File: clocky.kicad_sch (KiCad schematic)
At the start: 79 parts, among them J1 Bot 50 pin, J2 Bot 40 pin, J3 Top 50 pin, J4 Top 40 pin, J5 Power, J6 CAP, J8 Skedd, U1 HEF4094B, U10 TMP117xxDRV, U11 ENS220, U2 HEF4094B, U3 HEF4094B, U4 HEF4094B, U5 HEF4094B, U6 HEF4094B, U7 BQ25570, U8 ENS212, U9 STM32U031C8Ux, U98 TMP117xxDRV, U99 TMP117xxDRV, Y1 32768Hz

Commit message: Update PCB layout.  Song and dance with Kicad breaking footprints...
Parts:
- U7: footprint Package_DFN_QFN:QFN-20-1EP_3.5x3.5mm_P0.5mm_EP2x2mm -> Parts:QFN-20-1EP_3.5x3.5mm_P0.5mm_EP2x2mm
- U9: footprint Package_DFN_QFN:QFN-48-1EP_7x7mm_P0.5mm_EP5.6x5.6mm -> Parts:QFN-48-1EP_7x7mm_P0.5mm_EP5.6x5.6mm
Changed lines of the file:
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@@
 			)
 		)
-		(property "Footprint" "Package_DFN_QFN:QFN-48-1EP_7x7mm_P0.5mm_EP5.6x5.6mm"
+		(property "Footprint" "Parts:QFN-48-1EP_7x7mm_P0.5mm_EP5.6x5.6mm"
 			(at 49.53 157.48 0)
 			(effects
@@
 			)
 		)
-		(property "Footprint" "Package_DFN_QFN:QFN-20-1EP_3.5x3.5mm_P0.5mm_EP2x2mm"
+		(property "Footprint" "Parts:QFN-20-1EP_3.5x3.5mm_P0.5mm_EP2x2mm"
 			(at 67.31 53.34 0)
 			(effects

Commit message: Manufacturing updates.
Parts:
- C16: JLCPCB (none) -> C15195; LCSC C15195 -> (none)
- C8: JLCPCB C15850 -> C19702
- R25: value 330k -> 560k; JLCPCB C22807 -> C23203
- U11, U8: now left out of the parts list
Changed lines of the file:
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@@
 			)
 		)
-		(property "LCSC" "C15195"
+		(property "JLCPCB" "C15195"
 			(at 87.63 156.21 0)
 			(effects
@@
 			)
 		)
-		(property "JLCPCB" "C15850"
+		(property "JLCPCB" "C19702"
 			(at 58.42 24.13 0)
 			(effects
@@
 			)
 		)
-		(property "Sim.Pins" "1=K 2=A"
-			(at 96.52 124.46 0)
-			(effects
-				(font
-					(size 1.27 1.27)
-				)
-				(hide yes)
-			)
-		)
 		(property "JLCPCB" "C2290"
 			(at 96.52 124.46 0)
@@
 		(unit 1)
 		(exclude_from_sim no)
-		(in_bom yes)
+		(in_bom no)
 		(on_board yes)
 		(dnp no)
@@
 			)
 		)
-		(property "Value" "330k"
+		(property "Value" "560k"
 			(at 119.38 50.8 90)
 			(effects
@@
 			)
 		)
-		(property "JLCPCB" "C22807"
+		(property "JLCPCB" "C23203"
 			(at 119.38 50.8 0)
 			(effects
@@
 		(unit 1)
 		(exclude_from_sim no)
-		(in_bom yes)
+		(in_bom no)
 		(on_board yes)
 		(dnp no)

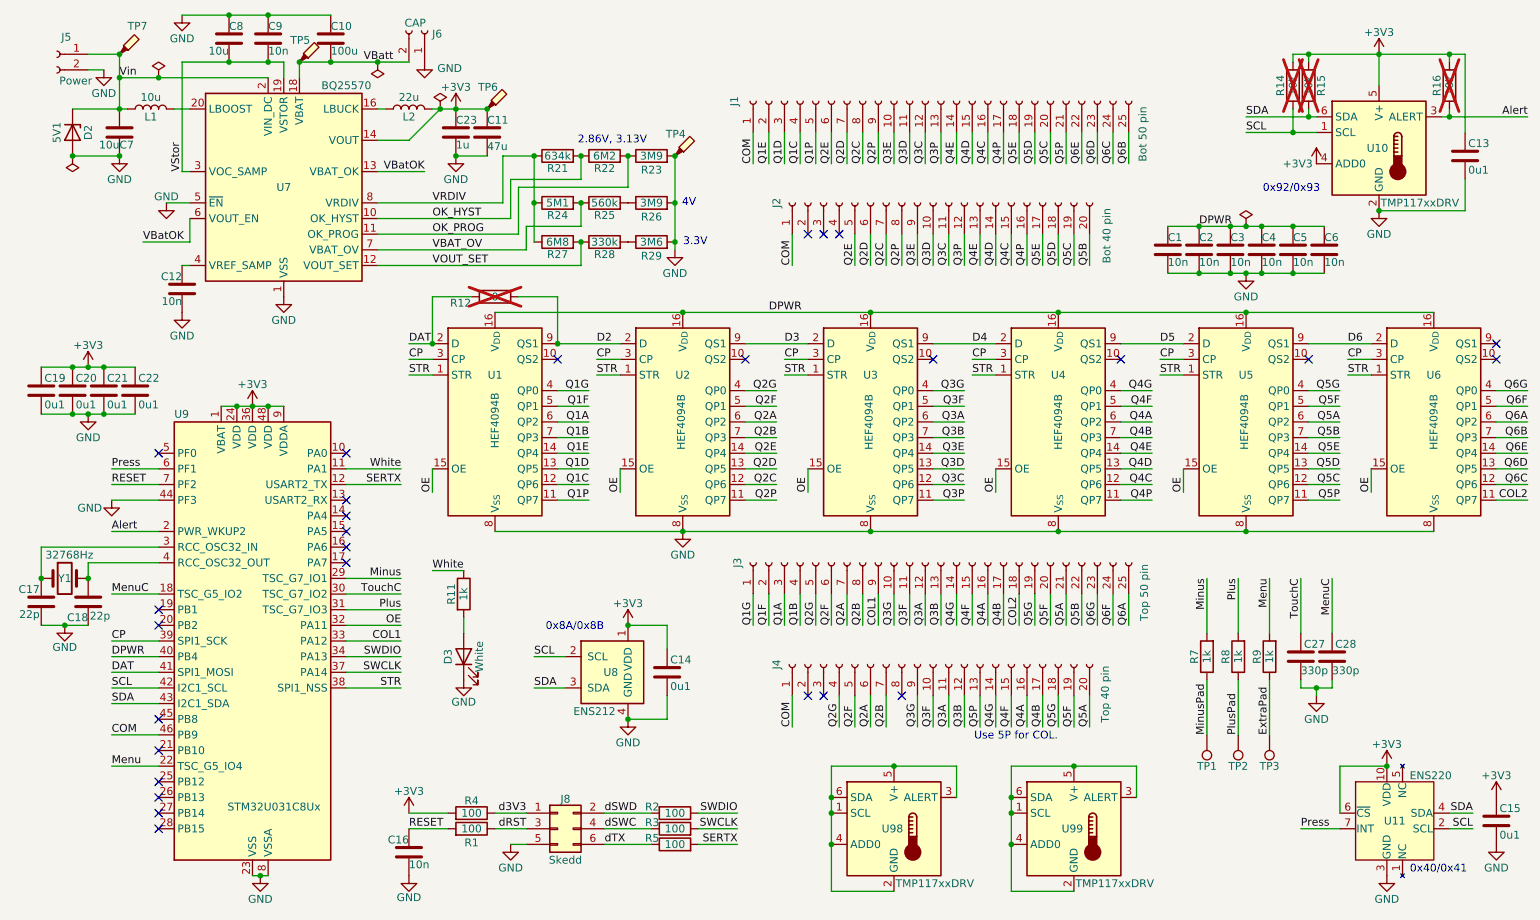
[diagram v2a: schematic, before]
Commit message: Update board with 1.8V power domain.
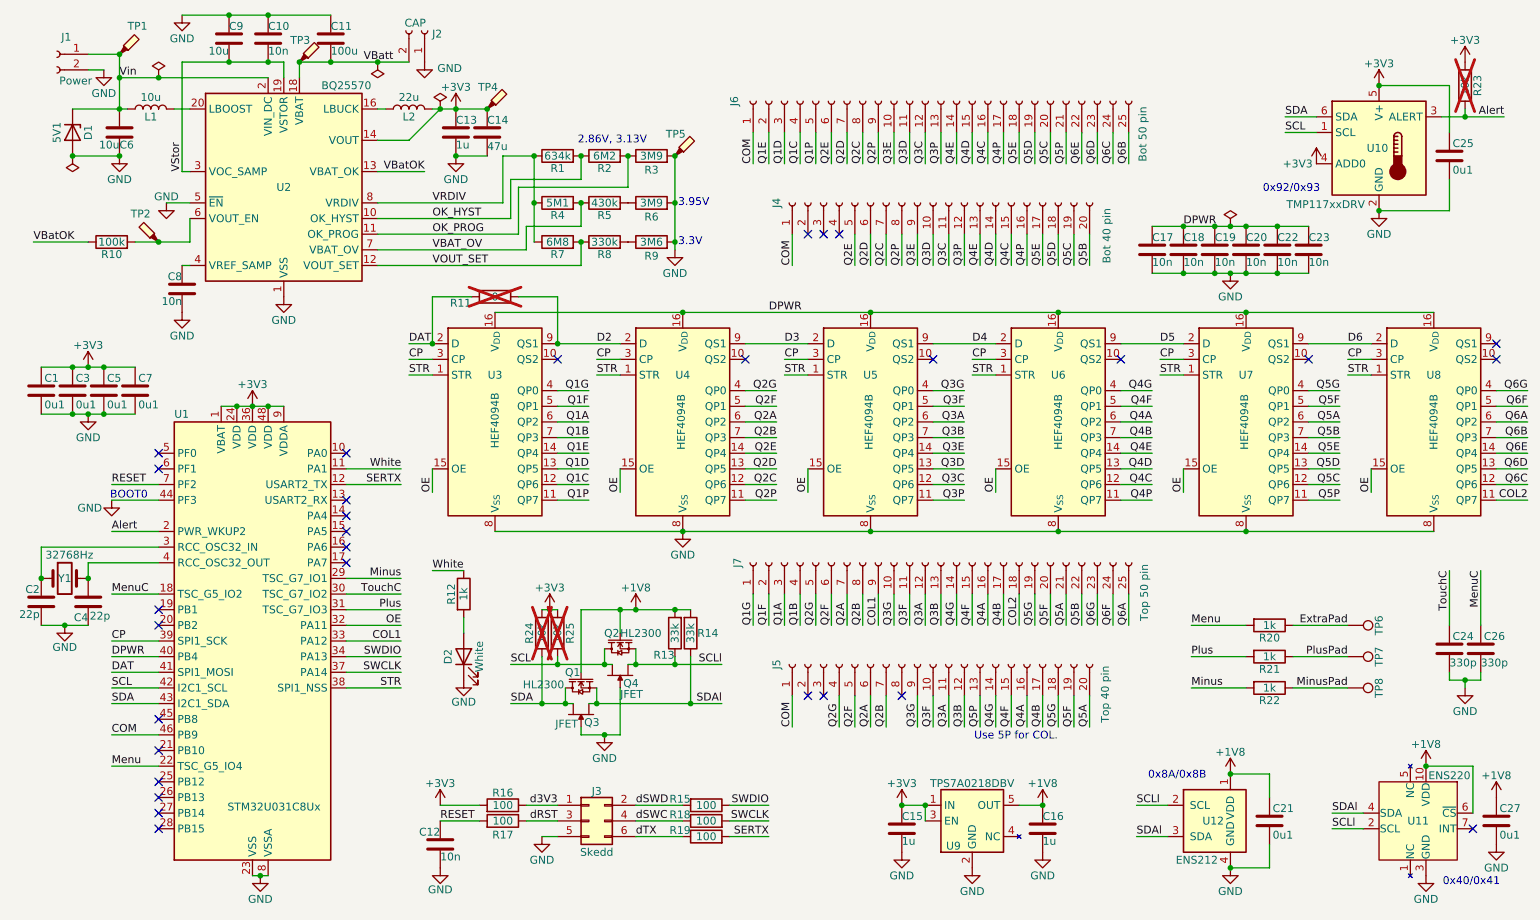
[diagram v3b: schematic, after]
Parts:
- removed U98, U99: TMP117xxDRV, Parts:WSON-6-1EP_2x2mm_P0.65mm_NoEP, symbol Sensor_Temperature:TMP117xxDRV
- added C15, C16: 1u, Capacitor_SMD:C_0402_1005Metric, symbol Device:C
- added Q1, Q2: HL2300, Package_TO_SOT_SMD:SOT-23, symbol Parts:HL2300
- added Q3, Q4: JFET, Package_TO_SOT_SMD:SOT-23-3, symbol Parts:Q_NJFET_DSG
- added R10: 100k, Resistor_SMD:R_0402_1005Metric, symbol Device:R
- added R13, R14: 33k, Resistor_SMD:R_0603_1608Metric, symbol Device:R
- added TP2: TestPoint_Probe, Parts:TestPoint, symbol Connector:TestPoint_Probe
- added U9: TPS7A0218DBV, Package_TO_SOT_SMD:SOT-23-5, symbol Parts:TPS7A0218DBV
- R5: renamed from R25; value 560k -> 430k
- U10: now left out of the parts list
- U2: renamed from U7; now left out of the parts list
- renumbered C19 to C1, C9 to C10, C10 to C11, C16 to C12, C23 to C13, C11 to C14, C1 to C17, C2 to C18, C3 to C19, C17 to C2, C4 to C20, C14 to C21, C5 to C22, C6 to C23, C27 to C24, C13 to C25, C28 to C26, C15 to C27, C20 to C3, C18 to C4, C21 to C5, C7 to C6, C22 to C7, C12 to C8, C8 to C9, D2 to D1, D3 to D2, J5 to J1, J6 to J2, J8 to J3, J2 to J4, J4 to J5, J1 to J6, J3 to J7, R21 to R1, R12 to R11, R11 to R12, R2 to R15, R4 to R16, R1 to R17, R3 to R18, R5 to R19, R22 to R2, R9 to R20, R8 to R21, R7 to R22, R16 to R23, R15 to R24, R14 to R25, R23 to R3, R24 to R4, R26 to R6, R27 to R7, R28 to R8, R29 to R9, TP7 to TP1, TP5 to TP3, TP6 to TP4, TP4 to TP5, TP3 to TP6, TP2 to TP7, TP1 to TP8, U9 to U1, U8 to U12, U1 to U3, U2 to U4, U3 to U5, U4 to U6, U5 to U7, U6 to U8
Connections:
- net +3V3: now also C15.1, U9.1 (IN), U9.3 (EN); no longer C21.1, C27.1, U11.10 (VDD), U11.6 (~{CS}), U12.1 (VDD)
- net GND: now also C15.2, C16.2, Q3.3 (G), Q4.3 (G), U9.2 (GND)
- net SCL: now also Q2.3 (D), Q4.2 (S); no longer U11.2 (SCL), U12.2 (SCL)
- net SDA: now also Q1.3 (D), Q3.1 (D); no longer U11.4 (SDA), U12.3 (SDA)
- net VBatOK: now also R10.1; no longer U2.6 (VOUT_EN)
- net Press: no longer names the net of U1.6 (PF1)
- net Press: no longer U11.7 (INT)
- new net: R10.2, TP2.1, U2.6 (VOUT_EN)
- new net +1V8: C16.1, C21.1, C27.1, Q1.1 (G), Q2.1 (G), R13.2, R14.2, U11.10 (VDD), U11.6 (~{CS}), U12.1 (VDD), U9.5 (OUT)
- new net SCLl: Q2.2 (S), Q4.1 (D), R13.1, U11.2 (SCL), U12.2 (SCL)
- new net SDAl: Q1.2 (S), Q3.2 (S), R14.1, U11.4 (SDA), U12.3 (SDA)
- no-connect marks 28 -> 30
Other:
- note added: "3.95V"
- note added: "BOOT0"
- note removed: "4V"
- moved on the sheet: C12, C17, C18, C19, C20, C21, C22, C23, C24, C25, C26, J3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

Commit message: Tweak a component.
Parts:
- R5: JLCPCB C23203 -> C25969
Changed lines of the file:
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@@
 			)
 		)
-		(property "JLCPCB" "C23203"
+		(property "JLCPCB" "C25969"
 			(at 119.38 50.8 0)
 			(effects
